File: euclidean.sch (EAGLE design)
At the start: 62 parts, among them IC1 LM324N, IC2 LM324N, IC3 LM324N, X1 CLOCK_IN, X10 TRIGGER OUT MASTER CLOCK, X2 TRIGGER OUT 0, X3 TRIGGER OUT 2, X4 TRIGGER OUT 4, X5 TRIGGER OUT 6, X6 TRIGGER OUT 1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

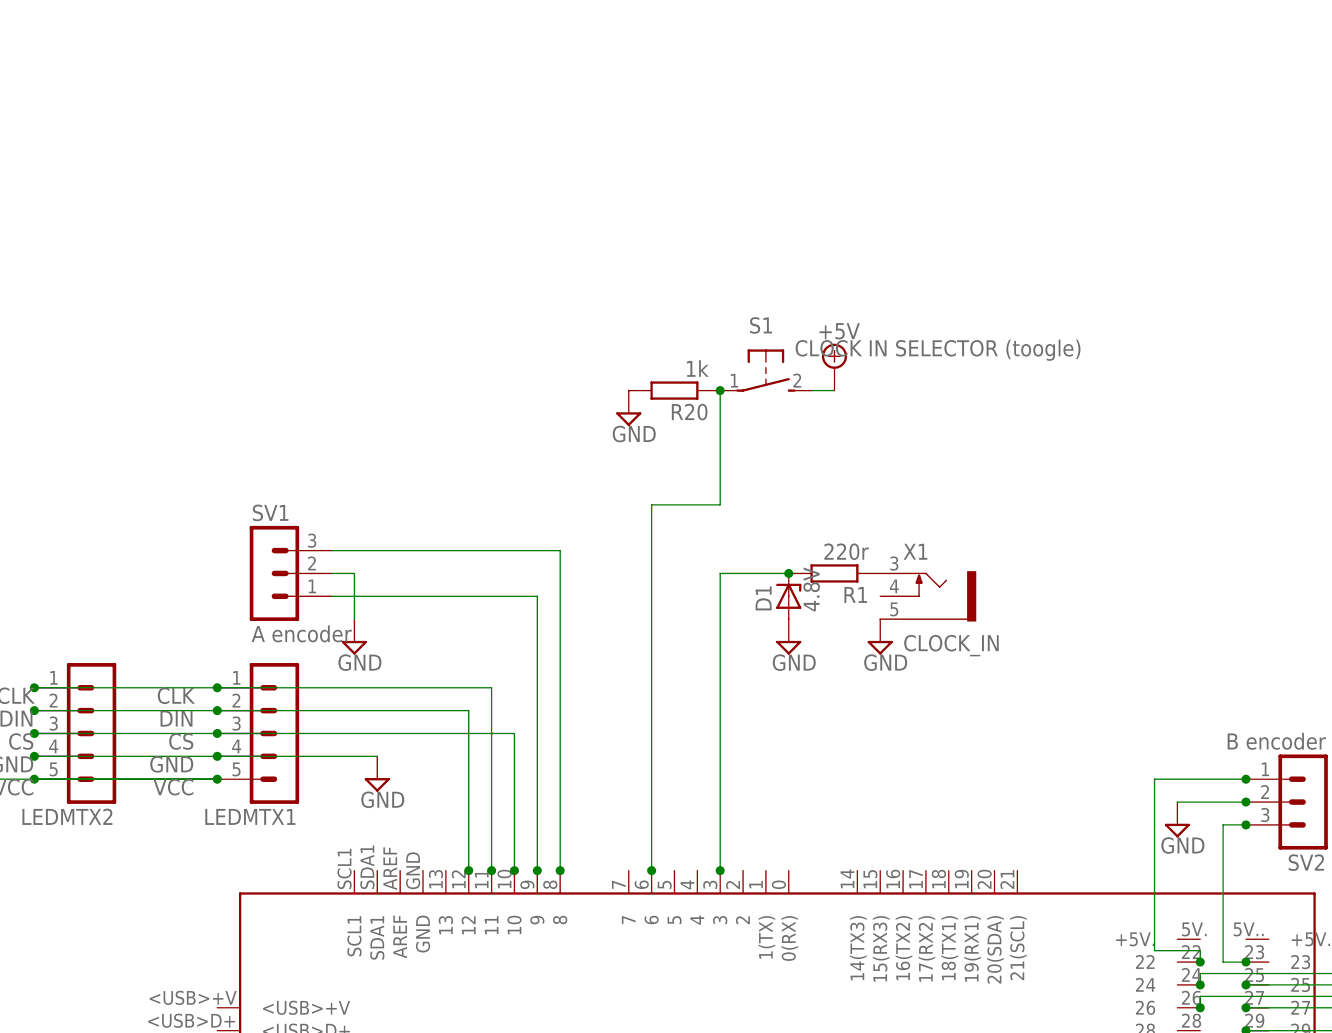
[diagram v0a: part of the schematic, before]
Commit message: New clock in circuit - better mc protection
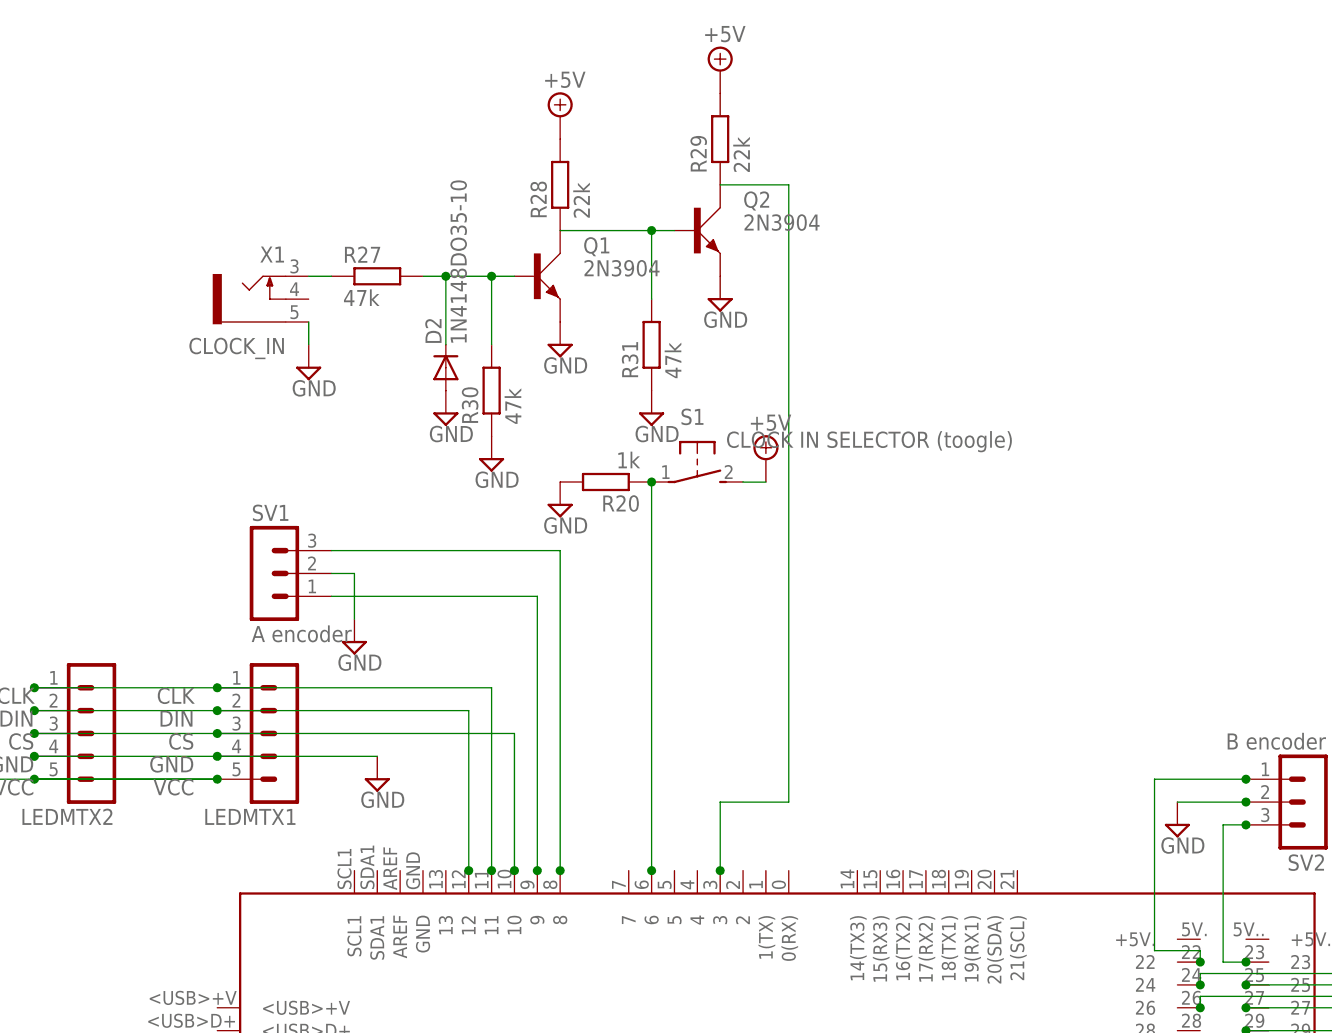
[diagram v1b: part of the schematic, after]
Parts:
- removed D1: 4.8V, diode:ZENER-DIODEZD-5
- removed R1: 220r, rcl:R-EU_0204/7
- added D2: 1N4148DO35-10, diode:1N4148DO35-10
- added Q1, Q2: 2N3904, transistor-small-signal:2N3904
- added R27, R30, R31: 47k, rcl:R-EU_0204/7
- added R28, R29: 22k, rcl:R-EU_0204/7
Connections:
- removed net N$7: D1.C, PCB1.3, R1.2
- new net N$55: D2.C, Q1.B, R27.2, R30.2
- new net N$57: Q1.C, Q2.B, R28.1, R31.2
- new net N$58: PCB1.3, Q2.C, R29.1
- net +5V: now also R28.2, R29.2
- net GND: now also D2.A, Q1.E, Q2.E, R30.1, R31.1; no longer D1.A
- net N$6: now also R27.1; no longer R1.1
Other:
- moved on the sheet: R20, S1, X1
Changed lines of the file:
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@@
 <part name="SUPPLY4" library="supply2" deviceset="GND" device=""/>
 <part name="X1" library="con-lumberg" deviceset="KLBR?" device="1" value="CLOCK_IN"/>
-<part name="D1" library="diode" deviceset="ZENER-DIODE" device="ZD-5" value="4.8V"/>
-<part name="R1" library="rcl" deviceset="R-EU_" device="0204/7" value="220r"/>
-<part name="SUPPLY5" library="supply2" deviceset="GND" device=""/>
 <part name="SUPPLY6" library="supply2" deviceset="GND" device=""/>
 <part name="IC1" library="linear" deviceset="LM324" device="N"/>
@@
 <part name="R26" library="rcl" deviceset="R-EU_" device="0204/7" value="1k"/>
 <part name="SUPPLY46" library="supply2" deviceset="GND" device=""/>
+<part name="R27" library="rcl" deviceset="R-EU_" device="0204/7" value="47k"/>
+<part name="D2" library="diode" deviceset="1N4148" device="DO35-10"/>
+<part name="Q1" library="transistor-small-signal" deviceset="2N3904" device=""/>
+<part name="Q2" library="transistor-small-signal" deviceset="2N3904" device=""/>
+<part name="R28" library="rcl" deviceset="R-EU_" device="0204/7" value="22k"/>
+<part name="R29" library="rcl" deviceset="R-EU_" device="0204/7" value="22k"/>
+<part name="R30" library="rcl" deviceset="R-EU_" device="0204/7" value="47k"/>
+<part name="R31" library="rcl" deviceset="R-EU_" device="0204/7" value="47k"/>
+<part name="SUPPLY47" library="supply2" deviceset="GND" device=""/>
+<part name="SUPPLY48" library="supply2" deviceset="GND" device=""/>
+<part name="SUPPLY49" library="supply2" deviceset="GND" device=""/>
+<part name="SUPPLY50" library="supply2" deviceset="GND" device=""/>
+<part name="SUPPLY51" library="supply2" deviceset="GND" device=""/>
+<part name="SUPPLY5" library="supply2" deviceset="+5V" device=""/>
+<part name="SUPPLY52" library="supply2" deviceset="+5V" device=""/>
 </parts>
 <sheets>
@@
 <instance part="SUPPLY3" gate="+5V" x="58.42" y="-2.54"/>
 <instance part="SUPPLY4" gate="GND" x="66.04" y="-5.08"/>
-<instance part="X1" gate="G$1" x="99.06" y="104.14"/>
-<instance part="D1" gate="G$1" x="83.82" y="104.14" rot="R90"/>
-<instance part="R1" gate="G$1" x="88.9" y="106.68" rot="R180"/>
-<instance part="SUPPLY5" gate="GND" x="83.82" y="99.06"/>
-<instance part="SUPPLY6" gate="GND" x="93.98" y="99.06"/>
+<instance part="X1" gate="G$1" x="25.4" y="137.16" rot="MR0"/>
+<instance part="SUPPLY6" gate="GND" x="30.48" y="129.54"/>
 <instance part="IC1" gate="A" x="182.88" y="35.56"/>
 <instance part="R2" gate="G$1" x="170.18" y="38.1" rot="R180"/>
@@
 <instance part="SUPPLY23" gate="GND" x="236.22" y="-45.72"/>
 <instance part="SUPPLY24" gate="GND" x="236.22" y="-76.2"/>
-<instance part="S1" gate="1" x="81.28" y="127" rot="R270"/>
-<instance part="SUPPLY25" gate="+5V" x="88.9" y="129.54"/>
-<instance part="R20" gate="G$1" x="71.12" y="127" rot="R180"/>
-<instance part="SUPPLY26" gate="GND" x="66.04" y="124.46"/>
+<instance part="S1" gate="1" x="73.66" y="116.84" rot="R270"/>
+<instance part="SUPPLY25" gate="+5V" x="81.28" y="119.38"/>
+<instance part="R20" gate="G$1" x="63.5" y="116.84" rot="R180"/>
+<instance part="SUPPLY26" gate="GND" x="58.42" y="114.3"/>
 <instance part="S2" gate="1" x="246.38" y="109.22" rot="R270"/>
 <instance part="SUPPLY27" gate="+5V" x="254" y="111.76"/>
@@
 <instance part="R26" gate="G$1" x="170.18" y="66.04" rot="R180"/>
 <instance part="SUPPLY46" gate="GND" x="165.1" y="63.5"/>
+<instance part="R27" gate="G$1" x="38.1" y="139.7"/>
+<instance part="D2" gate="G$1" x="45.72" y="129.54" rot="R90"/>
+<instance part="Q1" gate="1" x="55.88" y="139.7"/>
+<instance part="Q2" gate="1" x="73.66" y="144.78"/>
+<instance part="R28" gate="G$1" x="58.42" y="149.86" rot="R90"/>
+<instance part="R29" gate="G$1" x="76.2" y="154.94" rot="R90"/>
+<instance part="R30" gate="G$1" x="50.8" y="127" rot="R90"/>
+<instance part="R31" gate="G$1" x="68.58" y="132.08" rot="R90"/>
+<instance part="SUPPLY47" gate="GND" x="45.72" y="124.46"/>
+<instance part="SUPPLY48" gate="GND" x="50.8" y="119.38"/>
+<instance part="SUPPLY49" gate="GND" x="58.42" y="132.08"/>
+<instance part="SUPPLY50" gate="GND" x="68.58" y="124.46"/>
+<instance part="SUPPLY51" gate="GND" x="76.2" y="137.16"/>
+<instance part="SUPPLY5" gate="+5V" x="76.2" y="162.56"/>
+<instance part="SUPPLY52" gate="+5V" x="58.42" y="157.48"/>
 </instances>
 <busses>
@@
 <pinref part="S1" gate="1" pin="S"/>
 <pinref part="SUPPLY25" gate="+5V" pin="+5V"/>
-<wire x1="88.9" y1="127" x2="86.36" y2="127" width="0.1524" layer="91"/>
+<wire x1="81.28" y1="116.84" x2="78.74" y2="116.84" width="0.1524" layer="91"/>
 </segment>
 <segment>
@@
 <pinref part="SUPPLY45" gate="+5V" pin="+5V"/>
 <wire x1="187.96" y1="66.04" x2="185.42" y2="66.04" width="0.1524" layer="91"/>
+</segment>
+<segment>
+<pinref part="R29" gate="G$1" pin="2"/>
+<pinref part="SUPPLY5" gate="+5V" pin="+5V"/>
+</segment>
+<segment>
+<pinref part="R28" gate="G$1" pin="2"/>
+<pinref part="SUPPLY52" gate="+5V" pin="+5V"/>
 </segment>
 </net>
@@
 </segment>
 <segment>
-<pinref part="D1" gate="G$1" pin="A"/>
-<pinref part="SUPPLY5" gate="GND" pin="GND"/>
-</segment>
-<segment>
 <pinref part="X1" gate="G$1" pin="5"/>
 <pinref part="SUPPLY6" gate="GND" pin="GND"/>
+<wire x1="30.48" y1="134.62" x2="30.48" y2="132.08" width="0.1524" layer="91"/>
 </segment>
 <segment>
@@
 <pinref part="SUPPLY46" gate="GND" pin="GND"/>
 </segment>
-</net>
-<net name="N$6" class="0">
-<segment>
-<pinref part="X1" gate="G$1" pin="3"/>
-<pinref part="R1" gate="G$1" pin="1"/>
-</segment>
-</net>
-<net name="N$7" class="0">
-<segment>
-<pinref part="R1" gate="G$1" pin="2"/>
-<pinref part="D1" gate="G$1" pin="C"/>
-<wire x1="83.82" y1="106.68" x2="76.2" y2="106.68" width="0.1524" layer="91"/>
-<wire x1="76.2" y1="106.68" x2="76.2" y2="73.66" width="0.1524" layer="91"/>
-<pinref part="PCB1" gate="G$1" pin="3"/>
-<junction x="76.2" y="73.66"/>
-<junction x="83.82" y="106.68"/>
+<segment>
+<pinref part="D2" gate="G$1" pin="A"/>
+<pinref part="SUPPLY47" gate="GND" pin="GND"/>
+</segment>
+<segment>
+<pinref part="R30" gate="G$1" pin="1"/>
+<pinref part="SUPPLY48" gate="GND" pin="GND"/>
+</segment>
+<segment>
+<pinref part="Q1" gate="1" pin="E"/>
+<pinref part="SUPPLY49" gate="GND" pin="GND"/>
+</segment>
+<segment>
+<pinref part="R31" gate="G$1" pin="1"/>
+<pinref part="SUPPLY50" gate="GND" pin="GND"/>
+</segment>
+<segment>
+<pinref part="Q2" gate="1" pin="E"/>
+<pinref part="SUPPLY51" gate="GND" pin="GND"/>
 </segment>
 </net>
@@
 <pinref part="R20" gate="G$1" pin="1"/>
 <pinref part="PCB1" gate="G$1" pin="6"/>
-<wire x1="76.2" y1="127" x2="76.2" y2="114.3" width="0.1524" layer="91"/>
-<wire x1="76.2" y1="114.3" x2="68.58" y2="114.3" width="0.1524" layer="91"/>
-<wire x1="68.58" y1="114.3" x2="68.58" y2="73.66" width="0.1524" layer="91"/>
-<junction x="76.2" y="127"/>
+<wire x1="68.58" y1="116.84" x2="68.58" y2="73.66" width="0.1524" layer="91"/>
+<junction x="68.58" y="116.84"/>
 <junction x="68.58" y="73.66"/>
 </segment>
@@
 </segment>
 </net>
+<net name="N$6" class="0">
+<segment>
+<pinref part="X1" gate="G$1" pin="3"/>
+<pinref part="R27" gate="G$1" pin="1"/>
+<wire x1="30.48" y1="139.7" x2="33.02" y2="139.7" width="0.1524" layer="91"/>
+</segment>
+</net>
+<net name="N$55" class="0">
+<segment>
+<pinref part="R27" gate="G$1" pin="2"/>
+<pinref part="Q1" gate="1" pin="B"/>
+<wire x1="53.34" y1="139.7" x2="50.8" y2="139.7" width="0.1524" layer="91"/>
+<pinref part="R30" gate="G$1" pin="2"/>
+<wire x1="50.8" y1="139.7" x2="45.72" y2="139.7" width="0.1524" layer="91"/>
+<wire x1="45.72" y1="139.7" x2="43.18" y2="139.7" width="0.1524" layer="91"/>
+<wire x1="50.8" y1="132.08" x2="50.8" y2="139.7" width="0.1524" layer="91"/>
+<pinref part="D2" gate="G$1" pin="C"/>
+<wire x1="45.72" y1="132.08" x2="45.72" y2="139.7" width="0.1524" layer="91"/>
+<junction x="50.8" y="139.7"/>
+<junction x="45.72" y="139.7"/>
+</segment>
+</net>
+<net name="N$57" class="0">
+<segment>
+<pinref part="Q1" gate="1" pin="C"/>
+<pinref part="R28" gate="G$1" pin="1"/>
+<pinref part="Q2" gate="1" pin="B"/>
+<wire x1="58.42" y1="144.78" x2="68.58" y2="144.78" width="0.1524" layer="91"/>
+<pinref part="R31" gate="G$1" pin="2"/>
+<wire x1="68.58" y1="144.78" x2="71.12" y2="144.78" width="0.1524" layer="91"/>
+<wire x1="68.58" y1="137.16" x2="68.58" y2="144.78" width="0.1524" layer="91"/>
+<junction x="68.58" y="144.78"/>
+</segment>
+</net>
+<net name="N$58" class="0">
+<segment>
+<pinref part="Q2" gate="1" pin="C"/>
+<pinref part="R29" gate="G$1" pin="1"/>
+<wire x1="76.2" y1="149.86" x2="83.82" y2="149.86" width="0.1524" layer="91"/>
+<wire x1="83.82" y1="149.86" x2="83.82" y2="81.28" width="0.1524" layer="91"/>
+<wire x1="76.2" y1="81.28" x2="76.2" y2="73.66" width="0.1524" layer="91"/>
+<pinref part="PCB1" gate="G$1" pin="3"/>
+<junction x="76.2" y="73.66"/>
+<wire x1="83.82" y1="81.28" x2="76.2" y2="81.28" width="0.1524" layer="91"/>
+</segment>
+</net>
